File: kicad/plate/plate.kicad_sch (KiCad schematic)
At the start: 0 parts

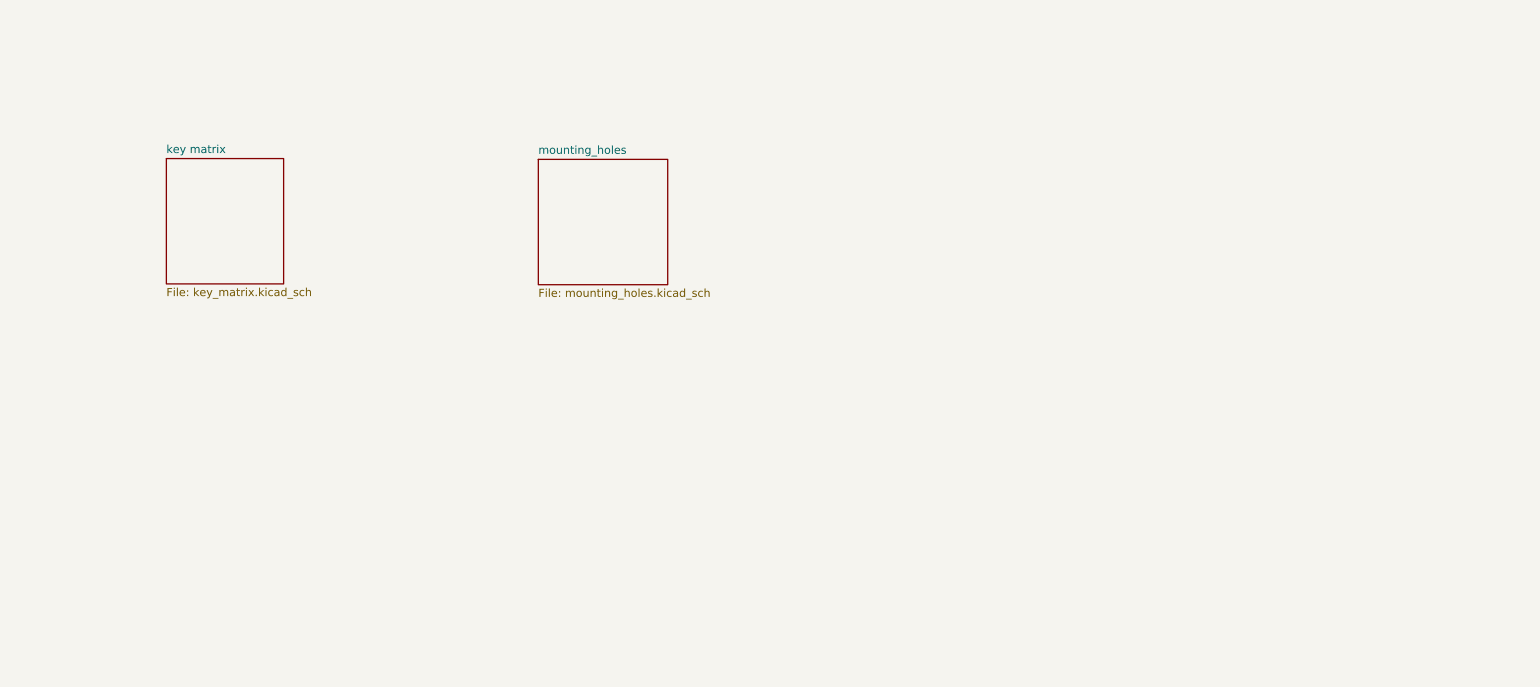
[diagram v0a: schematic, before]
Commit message: should be ok for proto order
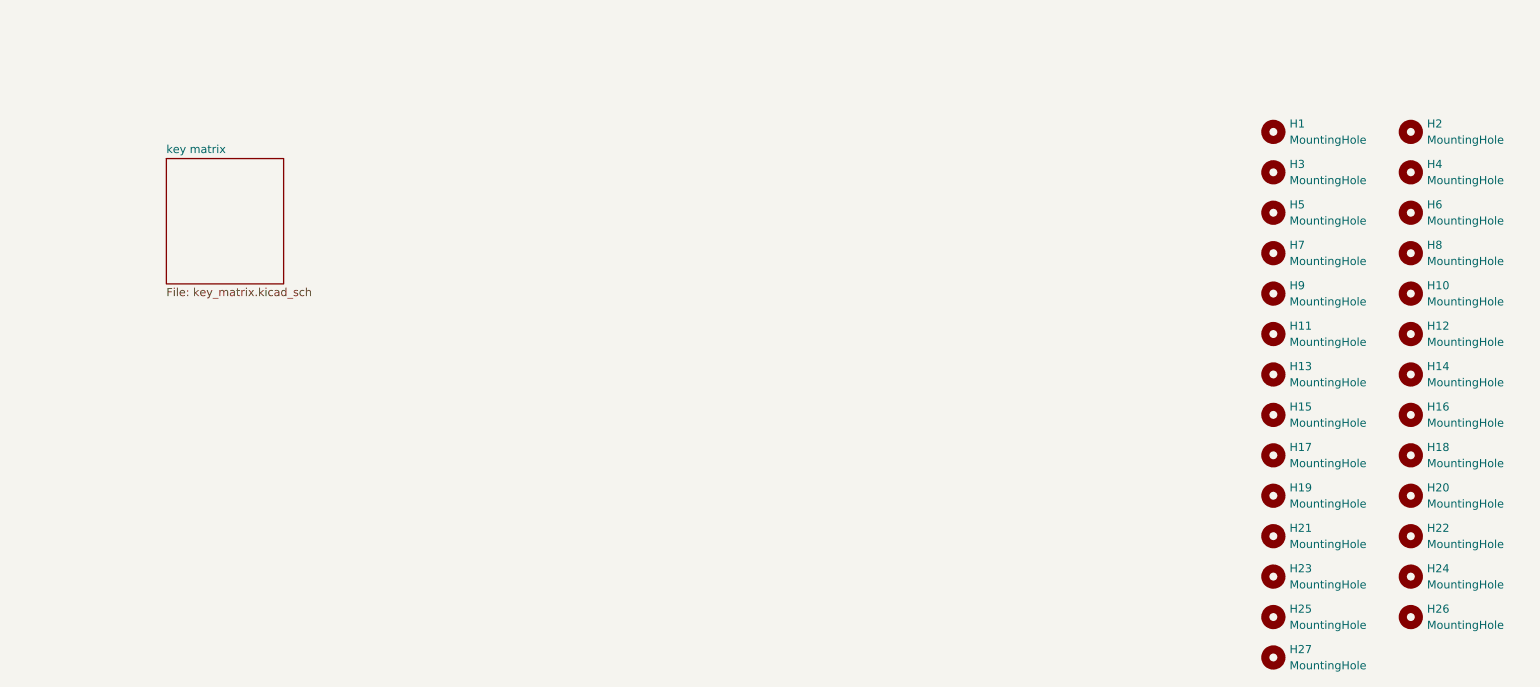
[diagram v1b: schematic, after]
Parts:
- added H1, H10, H11, H12, H13, H14, H15, H16, H17, H18, H19, H2, H20, H21, H22, H23, H24, H25, H26, H27, H3, H4, H5, H6, H7, H8, H9: MountingHole, MountingHole:MountingHole_3.2mm_M3_DIN965, symbol Mechanical:MountingHole
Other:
- removed sheet mounting_holes

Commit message: updated plate files
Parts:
- added SW1, SW10, SW11, SW12, SW13, SW14, SW15, SW16, SW17, SW18, SW19, SW2, SW20, SW21, SW22, SW23, SW24, SW25, SW27, SW28, SW29, SW3, SW30, SW31, SW32, SW33, SW34, SW35, SW36, SW37, SW38, SW39, SW4, SW40, SW43, SW44, SW45, SW5, SW6, SW7, SW8, SW9: SW_Push, capacitive_sensors:ec_plate_cutout_topre_14.1x14.7mm, symbol Switch:SW_Push
- added SW26, SW41, SW42: SW_Push, capacitive_sensors:ec_plate_cutout_topre_2u, symbol Switch:SW_Push
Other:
- removed sheet key matrix
